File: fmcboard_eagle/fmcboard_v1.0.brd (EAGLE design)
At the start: 98 x 74 mm, 39 parts, among them IC1 OPA699ID, IC2 OPA699ID, IC3 ICL7660CPA, IC4 ICL7660CPA, J1 8pin, J12 4p-2.54, J2 ASP-134604-01, J3 4p-2.54, J4 4p-2.54, J5 8pin, U1 TXS0108EPWR

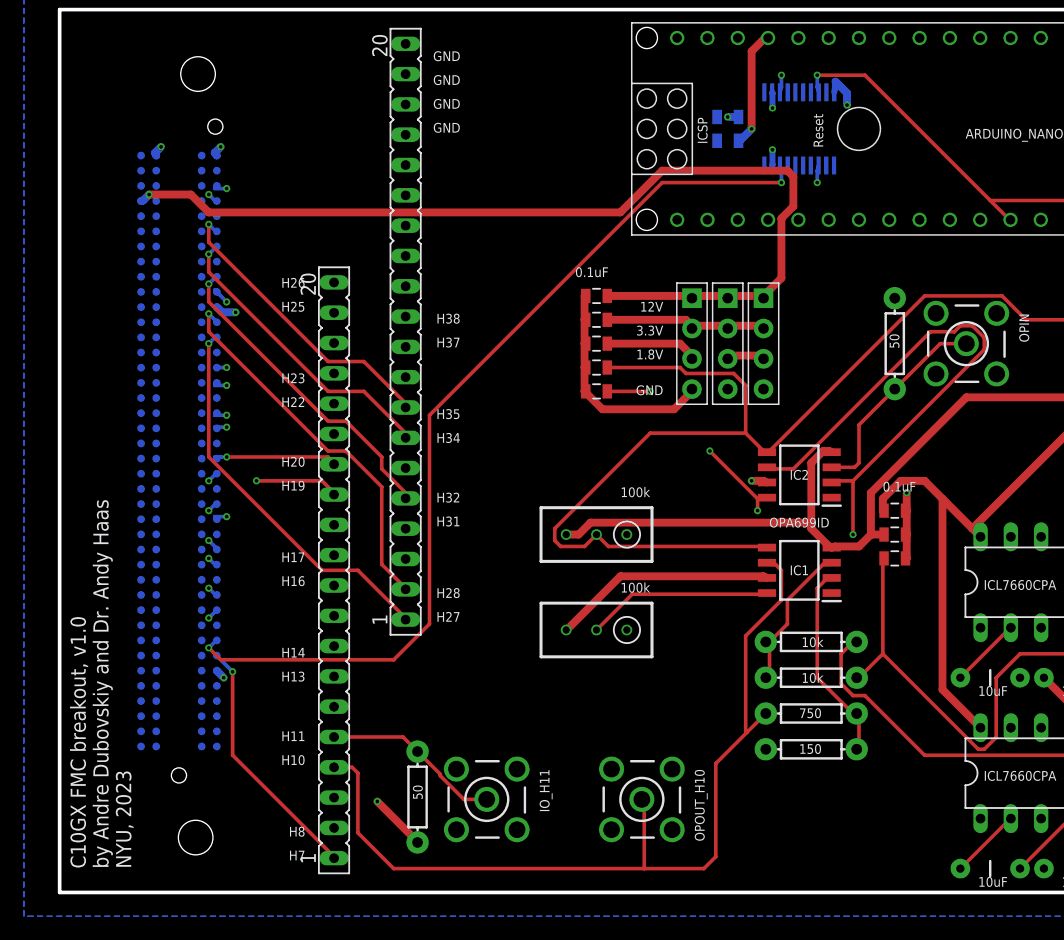
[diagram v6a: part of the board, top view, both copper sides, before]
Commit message: switch sda scl 5v to 1.8
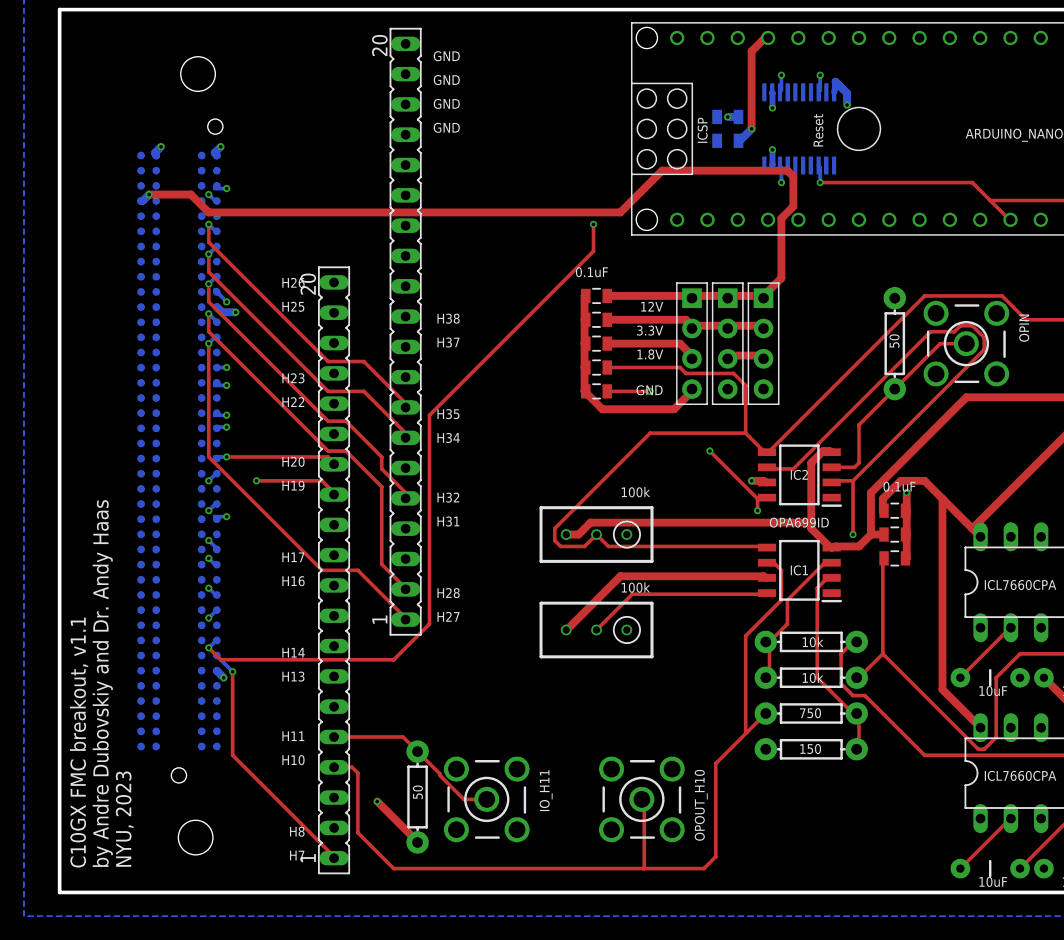
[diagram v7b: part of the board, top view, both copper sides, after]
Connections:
- net AR_SCLIN: now also U1.13; no longer U1.8
- net AR_SDAIN: now also U1.18; no longer U1.3
- net SCLIN: now also U1.8; no longer U1.13
- net SDAIN: now also U1.3; no longer U1.18
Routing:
- net SCLIN: track 108.6 -> 114.1 mm
- net SDAIN: track 97.0 -> 102.1 mm, vias 2 -> 3
- net AR_SCLIN: track 84.4 -> 80.4 mm
- net AR_SDAIN: track 84.6 -> 80.9 mm
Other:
- board text added: "C10GX FMC breakout, v1.1 by Andre Dubovskiy and Dr. Andy Haas NYU, 2023"
- board text removed: "C10GX FMC breakout, v1.0 by Andre Dubovskiy and Dr. Andy Haas NYU, 2023"
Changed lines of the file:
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@@
 <drawing>
 <settings>
-<setting alwaysvectorfont="yes"/>
+<setting alwaysvectorfont="no"/>
 <setting verticaltext="up"/>
 </settings>
@@
 <layers>
 <layer number="1" name="top" color="4" fill="1" visible="yes" active="yes"/>
-<layer number="2" name="topgnd" color="16" fill="1" visible="yes" active="yes"/>
+<layer number="2" name="topgnd" color="16" fill="1" visible="no" active="yes"/>
 <layer number="3" name="Route3" color="4" fill="3" visible="no" active="no"/>
 <layer number="4" name="Route4" color="1" fill="4" visible="no" active="no"/>
@@
 <layer number="14" name="Route14" color="1" fill="6" visible="no" active="no"/>
 <layer number="15" name="route" color="19" fill="1" visible="yes" active="yes"/>
-<layer number="16" name="gnd" color="1" fill="1" visible="yes" active="yes"/>
+<layer number="16" name="gnd" color="1" fill="1" visible="no" active="yes"/>
 <layer number="17" name="Pads" color="2" fill="1" visible="yes" active="yes"/>
 <layer number="18" name="Vias" color="2" fill="1" visible="yes" active="yes"/>
@@
 <text x="92.6" y="27.5" size="0.8128" layer="21" rot="R180">OPIN</text>
 <text x="92.6" y="52.5" size="0.8128" layer="21" rot="R180">GND</text>
-<text x="6" y="2" size="1.27" layer="21" rot="R90">C10GX FMC breakout, v1.0
+<text x="6" y="2" size="1.27" layer="21" rot="R90">C10GX FMC breakout, v1.1
 by Andre Dubovskiy and Dr. Andy Haas
 NYU, 2023</text>
@@
 <autorouter>
 <pass name="Default">
-<param name="RoutingGrid" value="0.25mm"/>
+<param name="RoutingGrid" value="0.125mm"/>
 <param name="AutoGrid" value="1"/>
 <param name="Efforts" value="1"/>
@@
 <param name="tpViaShape" value="round"/>
 <param name="PrefDir.1" value="*"/>
-<param name="PrefDir.2" value="0"/>
+<param name="PrefDir.2" value="*"/>
 <param name="PrefDir.3" value="0"/>
 <param name="PrefDir.4" value="0"/>
@@
 <contactref element="J2" pad="H8"/>
 <contactref element="SV1" pad="2"/>
-<contactref element="U1" pad="18"/>
 <wire x1="12.5" y1="20.5" x2="13" y2="21" width="0.3048" layer="16"/>
 <wire x1="12.5" y1="16" x2="12.5" y2="20.5" width="0.3048" layer="15"/>
@@
 <wire x1="13" y1="21" x2="13.175" y2="21.125" width="0.3048" layer="16"/>
 <wire x1="23" y1="5.5" x2="23" y2="5.41" width="0.3048" layer="15"/>
-<wire x1="60.5" y1="59.5" x2="60.5" y2="60.5" width="0.3048" layer="16"/>
-<wire x1="50.5" y1="59.5" x2="60.5" y2="59.5" width="0.3048" layer="1"/>
-<wire x1="31" y1="40" x2="50.5" y2="59.5" width="0.3048" layer="1"/>
 <wire x1="31" y1="22.5" x2="31" y2="40" width="0.3048" layer="1"/>
 <wire x1="28" y1="19.5" x2="31" y2="22.5" width="0.3048" layer="1"/>
 <wire x1="13.5" y1="19.5" x2="28" y2="19.5" width="0.3048" layer="1"/>
 <wire x1="12.5" y1="20.5" x2="13.5" y2="19.5" width="0.3048" layer="1"/>
-<wire x1="60.5" y1="60.5" x2="60.375" y2="60.935" width="0.3048" layer="16"/>
 <via x="12.5" y="20.5" extent="1-16" drill="0.3048"/>
-<via x="60.5" y="59.5" extent="1-16" drill="0.3048"/>
+<contactref element="U1" pad="3"/>
+<wire x1="60.5" y1="68.5" x2="60.5" y2="67.25" width="0.3048" layer="16"/>
+<wire x1="57.25" y1="68.5" x2="60.5" y2="68.5" width="0.3048" layer="15"/>
+<wire x1="44.75" y1="56" x2="57.25" y2="68.5" width="0.3048" layer="15"/>
+<wire x1="44.75" y1="53.75" x2="44.75" y2="56" width="0.3048" layer="1"/>
+<wire x1="31" y1="40" x2="44.75" y2="53.75" width="0.3048" layer="1"/>
+<wire x1="60.5" y1="67.25" x2="60.375" y2="67.065" width="0.3048" layer="16"/>
+<via x="60.5" y="68.5" extent="1-16" drill="0.3048"/>
+<via x="44.75" y="56" extent="1-16" drill="0.3048"/>
 </signal>
 <signal name="H13">
@@
 <contactref element="J2" pad="H7"/>
 <contactref element="SV1" pad="1"/>
-<contactref element="U1" pad="13"/>
 <wire x1="14.5" y1="18.5" x2="13" y2="20" width="0.3048" layer="16"/>
 <wire x1="14.5" y1="11.5" x2="14.5" y2="18.5" width="0.3048" layer="1"/>
@@
 <wire x1="13" y1="20" x2="13.175" y2="19.855" width="0.3048" layer="16"/>
 <wire x1="23" y1="3" x2="23" y2="2.87" width="0.3048" layer="1"/>
-<wire x1="63.5" y1="59.5" x2="63.5" y2="60.5" width="0.3048" layer="16"/>
-<wire x1="58" y1="65" x2="63.5" y2="59.5" width="0.3048" layer="15"/>
-<wire x1="55.5" y1="62.5" x2="58" y2="65" width="0.3048" layer="15"/>
-<wire x1="55.5" y1="52" x2="55.5" y2="62.5" width="0.3048" layer="15"/>
-<wire x1="57" y1="50.5" x2="55.5" y2="52" width="0.3048" layer="15"/>
 <wire x1="57" y1="38" x2="57" y2="50.5" width="0.3048" layer="15"/>
 <wire x1="31" y1="12" x2="57" y2="38" width="0.3048" layer="15"/>
 <wire x1="31" y1="11" x2="31" y2="12" width="0.3048" layer="15"/>
 <wire x1="23" y1="3" x2="31" y2="11" width="0.3048" layer="15"/>
-<wire x1="63.5" y1="60.5" x2="63.61" y2="60.935" width="0.3048" layer="16"/>
 <wire x1="23" y1="3" x2="23" y2="2.87" width="0.3048" layer="15"/>
 <via x="14.5" y="18.5" extent="1-16" drill="0.3048"/>
-<via x="63.5" y="59.5" extent="1-16" drill="0.3048"/>
+<contactref element="U1" pad="8"/>
+<wire x1="63.75" y1="68.5" x2="63.75" y2="67.25" width="0.3048" layer="16"/>
+<wire x1="64.5" y1="68.5" x2="63.75" y2="68.5" width="0.3048" layer="15"/>
+<wire x1="66.75" y1="66.25" x2="64.5" y2="68.5" width="0.3048" layer="15"/>
+<wire x1="66.75" y1="65.75" x2="66.75" y2="66.25" width="0.3048" layer="15"/>
+<wire x1="65.75" y1="64.75" x2="66.75" y2="65.75" width="0.3048" layer="15"/>
+<wire x1="57.75" y1="64.75" x2="65.75" y2="64.75" width="0.3048" layer="15"/>
+<wire x1="55.75" y1="62.75" x2="57.75" y2="64.75" width="0.3048" layer="15"/>
+<wire x1="55.75" y1="51.75" x2="55.75" y2="62.75" width="0.3048" layer="15"/>
+<wire x1="57" y1="50.5" x2="55.75" y2="51.75" width="0.3048" layer="15"/>
+<wire x1="63.75" y1="67.25" x2="63.625" y2="67.065" width="0.3048" layer="16"/>
+<via x="63.75" y="68.5" extent="1-16" drill="0.3048"/>
 </signal>
 <signal name="AR_SDAIN">
-<contactref element="U1" pad="3"/>
 <contactref element="J5" pad="6"/>
 <contactref element="ARDUINO_NANO1" pad="29"/>
-<wire x1="60.5" y1="68.5" x2="60.5" y2="67.5" width="0.3048" layer="16"/>
-<wire x1="62.5" y1="68.5" x2="60.5" y2="68.5" width="0.3048" layer="15"/>
-<wire x1="64" y1="67" x2="62.5" y2="68.5" width="0.3048" layer="15"/>
-<wire x1="74" y1="67" x2="64" y2="67" width="0.3048" layer="15"/>
 <wire x1="84.5" y1="56.5" x2="83" y2="58" width="0.3048" layer="15"/>
-<wire x1="83" y1="58" x2="74" y2="67" width="0.3048" layer="15"/>
-<wire x1="60.5" y1="67.5" x2="60.375" y2="67.065" width="0.3048" layer="16"/>
 <wire x1="84.5" y1="56.5" x2="84.78" y2="56.38" width="0.3048" layer="15"/>
 <wire x1="96.5" y1="17" x2="95" y2="15.5" width="0.3048" layer="15"/>
@@
 <wire x1="83" y1="58" x2="91.5" y2="58" width="0.3048" layer="15"/>
 <wire x1="95" y1="15.5" x2="95" y2="15.3" width="0.3048" layer="15"/>
-<via x="60.5" y="68.5" extent="1-16" drill="0.3048"/>
+<contactref element="U1" pad="18"/>
+<wire x1="60.5" y1="59.5" x2="60.5" y2="60.75" width="0.3048" layer="16"/>
+<wire x1="62.75" y1="59.5" x2="60.5" y2="59.5" width="0.3048" layer="15"/>
+<wire x1="64.25" y1="58" x2="62.75" y2="59.5" width="0.3048" layer="15"/>
+<wire x1="83" y1="58" x2="64.25" y2="58" width="0.3048" layer="15"/>
+<wire x1="60.5" y1="60.75" x2="60.375" y2="60.935" width="0.3048" layer="16"/>
+<via x="60.5" y="59.5" extent="1-16" drill="0.3048"/>
 </signal>
 <signal name="AR_SCLIN">
-<contactref element="U1" pad="8"/>
 <contactref element="J5" pad="7"/>
 <contactref element="ARDUINO_NANO1" pad="27"/>
-<wire x1="63.5" y1="68.5" x2="63.5" y2="67.5" width="0.3048" layer="16"/>
-<wire x1="67.5" y1="68.5" x2="63.5" y2="68.5" width="0.3048" layer="1"/>
 <wire x1="79.5" y1="56.5" x2="78" y2="58" width="0.3048" layer="1"/>
-<wire x1="78" y1="58" x2="67.5" y2="68.5" width="0.3048" layer="1"/>
-<wire x1="63.5" y1="67.5" x2="63.625" y2="67.065" width="0.3048" layer="16"/>
 <wire x1="79.5" y1="56.5" x2="79.7" y2="56.38" width="0.3048" layer="1"/>
 <wire x1="96.5" y1="14.5" x2="95" y2="13" width="0.3048" layer="1"/>
@@
 <wire x1="78" y1="58" x2="92" y2="58" width="0.3048" layer="1"/>
 <wire x1="95" y1="13" x2="95" y2="12.76" width="0.3048" layer="1"/>
-<via x="63.5" y="68.5" extent="1-16" drill="0.3048"/>
+<contactref element="U1" pad="13"/>
+<wire x1="63.75" y1="59.5" x2="63.75" y2="60.75" width="0.3048" layer="16"/>
+<wire x1="76.5" y1="59.5" x2="63.75" y2="59.5" width="0.3048" layer="1"/>
+<wire x1="78" y1="58" x2="76.5" y2="59.5" width="0.3048" layer="1"/>
+<wire x1="63.75" y1="60.75" x2="63.61" y2="60.935" width="0.3048" layer="16"/>
+<via x="63.75" y="59.5" extent="1-16" drill="0.3048"/>
 </signal>
 <signal name="IO2_H11">

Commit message: Board v1.1
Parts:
- removed OPOUT_H10: BU-SMB-V, con-coax:BU-SMB-V
- added IO_G2, IO_G3, IO_H4, IO_H5: BU-SMB-V, con-coax:BU-SMB-V
- added R10, R12: 150, rcl:R0805
- added R11, R9: 750, rcl:R0805
- added R13, R14: 10k, rcl:R0805
- added R15, R16: 50, SparkFun-Resistors:AXIAL-0.3
- R1: value 750 -> 100k; device SparkFun-Resistors:AXIAL-0.3 -> resistor:RTRIM3296W
- R3: value 10k -> 100k; device SparkFun-Resistors:AXIAL-0.3 -> rcl:R0805
- R4: value 150 -> 50
- R5: value 10k -> 50
- moved R1 30.4 mm to (41.0, 36.0), turned to 90 degrees
- moved R3 21.6 mm to (51.0, 39.0)
- moved U1 21.6 mm to (41.0, 59.0), flipped to the top
- moved C9 17.5 mm to (39.0, 67.0), flipped to the top, turned to 180 degrees
- moved C14 17.0 mm to (39.0, 65.0), flipped to the top, turned to 180 degrees
- moved R5 13.9 mm to (56.0, 6.00), turned to 90 degrees
- moved R4 8.06 mm to (56.0, 16.0), turned to 90 degrees
- moved R7 4.47 mm to (41.0, 24.0)
- moved C10 4.00 mm to (70.0, 34.0)
- moved C11 4.00 mm to (70.0, 32.0)
- moved C3 4.00 mm to (70.0, 36.0)
- moved R8 4.00 mm to (41.0, 30.0)
- moved IC1 2.24 mm to (61.0, 25.0)
- moved IO_H11 2.00 mm to (35.8, 5.80)
- moved R6 2.00 mm to (30.0, 6.00)
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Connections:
- new net AR_G36: ARDUINO_NANO1.24, U1.16
- new net AR_G37: ARDUINO_NANO1.23, U1.15
- new net G2: IO_G2.1, J2.G2, R4.P$2, SV2.16
- new net G3: IO_G3.1, J2.G3, R5.P$2, SV2.17
- new net G36: J2.G36, U1.5
- new net G37: J2.G37, U1.6
- new net H4: IO_H4.1, J2.H4, R15.P$2, SV2.13
- new net H5: IO_H5.1, J2.H5, R16.P$2, SV2.14
- new net N$7: IC2.2, R11.1, R12.2
- new net N$8: R1.2, R3.2
- net +VS: now also R1.3
- net -VS: now also R1.1
- net GND: now also IO_G2.2, IO_G2.3, IO_G2.4, IO_G2.5, IO_G3.2, IO_G3.3, IO_G3.4, IO_G3.5, IO_H4.2, IO_H4.3, IO_H4.4, IO_H4.5, IO_H5.2, IO_H5.3, IO_H5.4, IO_H5.5, R10.1, R12.1, R15.P$1, R16.P$1, R4.P$1, R5.P$1; no longer OPOUT_H10.2, OPOUT_H10.3, OPOUT_H10.4, OPOUT_H10.5, R4.P$2, SV2.17
- net N$1: now also R13.1, R14.1; no longer R3.P$1, R5.P$1
- net N$3: now also R10.2, R9.1; no longer R1.P$2, R4.P$1
- net OFFSETIN1: now also R14.2, R3.1; no longer R5.P$2
- net OPBUF1: now also R11.2, R13.2; no longer IC2.2, R3.P$2
- net OPOUT1_H10: now also R9.2; no longer OPOUT_H10.1, R1.P$1
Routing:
- net G2: track 0.00 -> 137.0 mm, vias 0 -> 2
- net G3: track 0.00 -> 122.3 mm, vias 0 -> 1
- net H5: track 0.00 -> 114.9 mm, vias 0 -> 1
- net H4: track 0.00 -> 77.8 mm, vias 0 -> 2
- net G36: track 0.00 -> 50.1 mm, vias 0 -> 2
- net G37: track 0.00 -> 42.5 mm, vias 0 -> 1
- net OFFSETIN1: track 47.1 -> 86.9 mm
- net AR_G36: track 0.00 -> 33.1 mm, vias 0 -> 1
- net SCLIN: track 114.1 -> 81.5 mm, vias 2 -> 1
- net AR_G37: track 0.00 -> 31.0 mm, vias 0 -> 1
- net N$7: track 0.00 -> 24.5 mm
- net 12V: track 81.9 -> 64.5 mm
- net AR_SDAIN: track 80.9 -> 97.1 mm
- net OPBUF1: track 94.9 -> 79.9 mm, vias 1 -> 0
- net SDAIN: track 102.1 -> 87.8 mm, vias 3 -> 1
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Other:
- board text added: "G2"
- board text added: "G3"
- board text added: "H4"
- board text added: "H5"
